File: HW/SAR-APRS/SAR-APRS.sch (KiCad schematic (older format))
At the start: 46 parts, among them J1 uFl, J2 Prog_header, J3 USB_B_Micro, Q1 2N7002, U1 DRA818V, U2 arduino_mini_clone, U3 NEO_GPS_MODULE, U4 HC-05, U5 TP4056

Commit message: update
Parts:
- removed D3, D4: LED, symbol device:LED
- removed R10: 100k, symbol device:R_Small
- added C12, C?: 100nF, symbol device:C_Small
- added C13: 10uF, symbol device:C_Small
- added D?: LED_BGRA, symbol device:LED_BGRA
- added D?: LED, symbol device:LED
- added J4: uFl, w_conn_rf:coaxial_u.fl-r-smt-1, symbol Connector:Conn_Coaxial
- added L4: L_Small, symbol device:L_Small
- added R19: 100, symbol device:R_Small
- added R?: 1k, symbol device:R_Small
- added U6: NEO-M8, symbol APRS_modules:NEO-M8
- added U?: EEPROM, symbol MLAB_IO:EEPROM
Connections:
- wire segments 166 -> 206
- no-connect marks 8 -> 17
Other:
- moved on the sheet: C1, C10, C11, C2, C3, C4, C5, C6, C7, C8, C9, D1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

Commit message: schematic update memmory adding
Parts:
- added C14: 100nF, symbol device:C_Small
- added U7: AT45DB641, Mlab_IO:SOIC-8_3.9x4.9mm_Pitch1.27mm, symbol APRS_modules:AT45DB081
- gave numbers to parts that had none: 5
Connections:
- wire segments 206 -> 222
- no-connect marks 17 -> 18
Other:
- moved on the sheet: C5
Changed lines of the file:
@@
 	6650 3525 6375 3525
 Wire Wire Line
-	5375 1600 6650 1600
-Wire Wire Line
-	5175 1600 4900 1600
+	5200 1600 6650 1600
+Wire Wire Line
+	5000 1600 4900 1600
 $Comp
 L device:C_Small C5
 U 1 1 5C01262D
-P 5275 1600
-F 0 "C5" H 5367 1646 50  0000 L CNN
-F 1 "10uF" H 5367 1555 50  0000 L CNN
-F 2 "" H 5275 1600 50  0001 C CNN
-F 3 "~" H 5275 1600 50  0001 C CNN
-	1    5275 1600
+P 5100 1600
+F 0 "C5" H 5192 1646 50  0000 L CNN
+F 1 "10uF" H 5192 1555 50  0000 L CNN
+F 2 "" H 5100 1600 50  0001 C CNN
+F 3 "~" H 5100 1600 50  0001 C CNN
+	1    5100 1600
 	0    -1   -1   0
 $EndComp
@@
 	6375 3125 6775 3125
 Wire Wire Line
-	6775 3125 6775 1600
-Wire Wire Line
-	6775 1600 9550 1600
-Wire Wire Line
-	9550 1600 9550 2525
+	6775 3125 6775 1775
+Wire Wire Line
+	6775 1775 9550 1775
+Wire Wire Line
+	9550 1775 9550 2525
 Wire Wire Line
 	8900 2525 9550 2525
@@
 Connection ~ 7500 5900
 $Comp
-L MLAB_IO:EEPROM U?
+L MLAB_IO:EEPROM U8
 U 1 1 5C17609F
 P 5825 6150
-F 0 "U?" H 5575 6550 60  0000 C CNN
+F 0 "U8" H 5575 6550 60  0000 C CNN
 F 1 "EEPROM" H 6150 6525 60  0000 C CNN
 F 2 "" H 5825 6150 60  0001 C CNN
@@
 $EndComp
 $Comp
-L device:LED_BGRA D?
+L device:LED_BGRA D4
 U 1 1 5C04ED53
 P 2275 6325
-F 0 "D?" V 2450 6650 50  0000 R CNN
+F 0 "D4" V 2450 6650 50  0000 R CNN
 F 1 "LED_BGRA" V 2275 7075 50  0000 R CNN
 F 2 "" H 2275 6275 50  0001 C CNN
@@
 	2725 6050 2825 6050
 $Comp
-L power:GND #PWR?
+L power:GND #PWR0134
 U 1 1 5C0E737B
 P 5825 6650
-F 0 "#PWR?" H 5825 6400 50  0001 C CNN
+F 0 "#PWR0134" H 5825 6400 50  0001 C CNN
 F 1 "GND" V 5830 6522 50  0000 R CNN
 F 2 "" H 5825 6650 50  0001 C CNN
@@
 $EndComp
 $Comp
-L power:+3V3 #PWR?
+L power:+3V3 #PWR0147
 U 1 1 5C0EEFDD
 P 5825 5500
-F 0 "#PWR?" H 5825 5350 50  0001 C CNN
+F 0 "#PWR0147" H 5825 5350 50  0001 C CNN
 F 1 "+3V3" H 5840 5673 50  0000 C CNN
 F 2 "" H 5825 5500 50  0001 C CNN
@@
 $EndComp
 $Comp
-L device:C_Small C?
+L device:C_Small C15
 U 1 1 5C0F65E9
 P 5600 5575
-F 0 "C?" H 5725 5650 50  0000 L CNN
+F 0 "C15" H 5725 5650 50  0000 L CNN
 F 1 "100nF" H 5675 5575 50  0000 L CNN
 F 2 "" H 5600 5575 50  0001 C CNN
@@
 	5825 5575 5825 5650
 $Comp
-L power:GND #PWR?
+L power:GND #PWR0148
 U 1 1 5C117D4C
 P 5500 5575
-F 0 "#PWR?" H 5500 5325 50  0001 C CNN
+F 0 "#PWR0148" H 5500 5325 50  0001 C CNN
 F 1 "GND" V 5505 5447 50  0000 R CNN
 F 2 "" H 5500 5575 50  0001 C CNN
@@
 	7950 5650 8025 5650
 $Comp
-L device:LED D?
+L device:LED D3
 U 1 1 5C189B26
 P 9750 5975
-F 0 "D?" V 9789 6053 50  0000 L CNN
+F 0 "D3" V 9789 6053 50  0000 L CNN
 F 1 "LED" V 9698 6053 50  0000 L CNN
 F 2 "" H 9750 5975 50  0001 C CNN
@@
 $EndComp
 $Comp
-L device:R_Small R?
+L device:R_Small R10
 U 1 1 5C193BD7
 P 9750 5725
-F 0 "R?" H 9600 5800 50  0000 L CNN
+F 0 "R10" H 9600 5800 50  0000 L CNN
 F 1 "1k" H 9600 5700 50  0000 L CNN
 F 2 "" H 9750 5725 50  0001 C CNN
@@
 $EndComp
 $Comp
-L power:GND #PWR?
+L power:GND #PWR0149
 U 1 1 5C199FCE
 P 9525 5150
-F 0 "#PWR?" H 9525 4900 50  0001 C CNN
+F 0 "#PWR0149" H 9525 4900 50  0001 C CNN
 F 1 "GND" V 9530 5022 50  0000 R CNN
 F 2 "" H 9525 5150 50  0001 C CNN
@@
 NoConn ~ 9525 5750
 $Comp
-L power:GND #PWR?
+L power:GND #PWR0150
 U 1 1 5C1E09BF
 P 9750 6125
-F 0 "#PWR?" H 9750 5875 50  0001 C CNN
+F 0 "#PWR0150" H 9750 5875 50  0001 C CNN
 F 1 "GND" V 9755 5997 50  0000 R CNN
 F 2 "" H 9750 6125 50  0001 C CNN
@@
 Wire Wire Line
 	8575 1900 8575 2425
+$Comp
+L power:GND #PWR0151
+U 1 1 5C1820F5
+P 8625 1175
+F 0 "#PWR0151" H 8625 925 50  0001 C CNN
+F 1 "GND" V 8625 1050 50  0000 R CNN
+F 2 "" H 8625 1175 50  0001 C CNN
+F 3 "" H 8625 1175 50  0001 C CNN
+	1    8625 1175
+	0    -1   1    0
+$EndComp
+$Comp
+L power:+3V3 #PWR0152
+U 1 1 5C18A0AD
+P 8875 1275
+F 0 "#PWR0152" H 8875 1125 50  0001 C CNN
+F 1 "+3V3" H 8890 1448 50  0000 C CNN
+F 2 "" H 8875 1275 50  0001 C CNN
+F 3 "" H 8875 1275 50  0001 C CNN
+	1    8875 1275
+	0    1    -1   0
+$EndComp
+$Comp
+L device:C_Small C14
+U 1 1 5C19098B
+P 8975 1550
+F 0 "C14" H 9067 1596 50  0000 L CNN
+F 1 "100nF" V 9125 1250 50  0000 L CNN
+F 2 "" H 8975 1550 50  0001 C CNN
+F 3 "~" H 8975 1550 50  0001 C CNN
+	1    8975 1550
+	0    -1   1    0
+$EndComp
+$Comp
+L power:GND #PWR0153
+U 1 1 5C245DAA
+P 7525 1375
+F 0 "#PWR0153" H 7525 1125 50  0001 C CNN
+F 1 "GND" V 7525 1225 50  0000 R CNN
+F 2 "" H 7525 1375 50  0001 C CNN
+F 3 "" H 7525 1375 50  0001 C CNN
+	1    7525 1375
+	0    1    -1   0
+$EndComp
+Wire Wire Line
+	6375 2925 6500 2925
+Wire Wire Line
+	5475 3025 5350 3025
+$Comp
+L APRS_modules:AT45DB081 U7
+U 1 1 5C2A166A
+P 8075 1225
+F 0 "U7" H 8075 1640 50  0000 C CNN
+F 1 "AT45DB641" H 8075 1549 50  0000 C CNN
+F 2 "Mlab_IO:SOIC-8_3.9x4.9mm_Pitch1.27mm" H 7525 1475 50  0001 C CNN
+F 3 "" H 7525 1475 50  0001 C CNN
+	1    8075 1225
+	1    0    0    -1
+$EndComp
+NoConn ~ 8625 1375
+Wire Wire Line
+	8625 1275 8800 1275
+Wire Wire Line
+	8875 1550 8800 1550
+Connection ~ 8800 1275
+Wire Wire Line
+	8800 1275 8875 1275
+$Comp
+L power:GND #PWR0154
+U 1 1 5C302407
+P 9075 1550
+F 0 "#PWR0154" H 9075 1300 50  0001 C CNN
+F 1 "GND" V 9075 1425 50  0000 R CNN
+F 2 "" H 9075 1550 50  0001 C CNN
+F 3 "" H 9075 1550 50  0001 C CNN
+	1    9075 1550
+	0    -1   1    0
+$EndComp
+Wire Wire Line
+	7525 1275 7175 1275
+Wire Wire Line
+	7175 1275 7175 1550
+Wire Wire Line
+	7175 1550 8800 1550
+Connection ~ 8800 1550
+Wire Wire Line
+	8800 1550 8800 1275
+Wire Wire Line
+	6500 1175 7525 1175
+Wire Wire Line
+	7525 1075 5475 1075
+Wire Wire Line
+	5350 750  8625 750
+Wire Wire Line
+	8625 750  8625 1075
+Wire Wire Line
+	5350 750  5350 3025
+Wire Wire Line
+	5475 1075 5475 2925
+Wire Wire Line
+	6500 1175 6500 2925
 $EndSCHEMATC

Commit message: schematic update
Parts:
- removed R15: ?, symbol device:R_Small
- removed R16: 1k, symbol device:R_Small
- removed U5: TP4056, symbol APRS_modules:TP4056
- added C? (x2): 100nF, symbol device:C_Small
- added Q? (x2): 2N7002, TO_SOT_Packages_SMD:SOT-23, symbol Transistor:2N7002
- added R?: 100, symbol device:R_Small
- added R?: 1k, symbol device:R_Small
- added U?: DW01x, symbol APRS_modules:DW01x
- added U?: TP4056, symbol APRS_modules:TP4056
- R14: value 1k -> 1k2
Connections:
- net labels removed: Temp
- wire segments 222 -> 231
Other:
- moved on the sheet: C10, C11, D4, J3, R13, R14, R17, R18

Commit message: schematic update
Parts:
- removed C10: 10uF, symbol device:C_Small
- added C10, C18: 10uF, symbol device:CP1_Small
- added D5: 1N5818, Diode_THT:D_DO-41_SOD81_P10.16mm_Horizontal, symbol Diode:1N5818
- added L5: 22uH, symbol device:L_Small
- added R20: ?, symbol device:R_Small
- added R21: 2k4, symbol device:R_Small
- added R22: 1k5, symbol device:R_Small
- added U10: ADP1108AN-3.3, Housings_DIP:DIP-8_W7.62mm, symbol dc-dc:ADP1108AN-3.3
- gave numbers to parts that had none: 8
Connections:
- net labels removed: +3V8
- wire segments 231 -> 255
- no-connect marks 18 -> 21
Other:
- moved on the sheet: C1, C11, C12, C13, C14, C15, C16, C17, C2, C3, C4, C5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

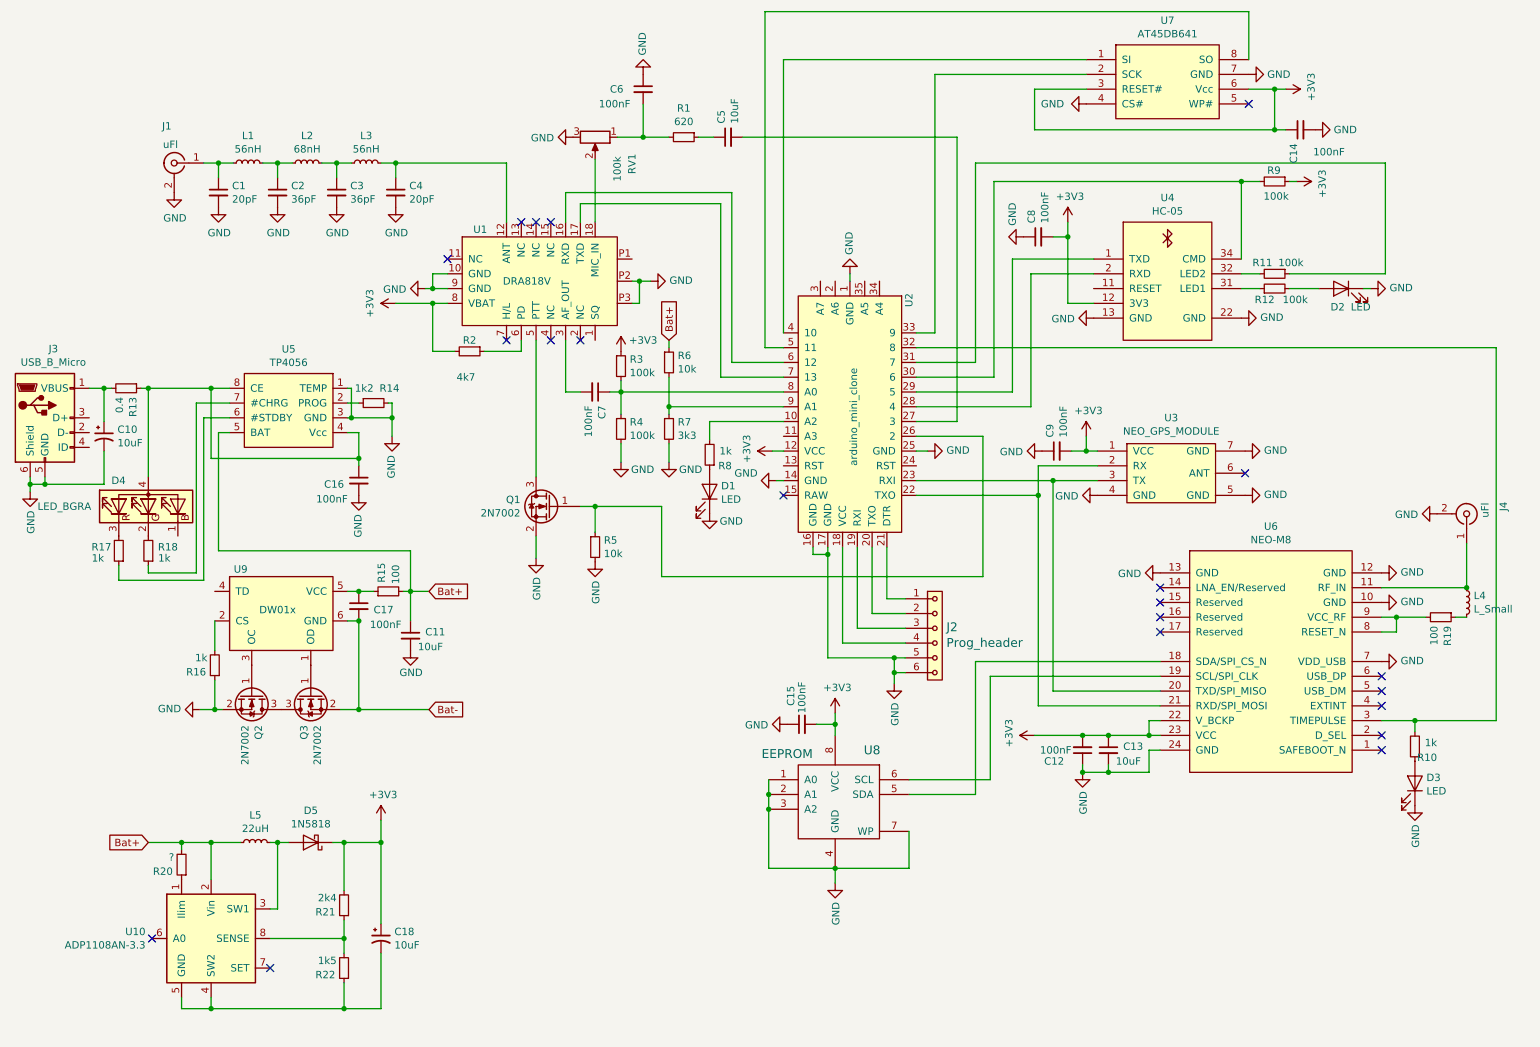
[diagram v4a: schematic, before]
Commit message: schematic update
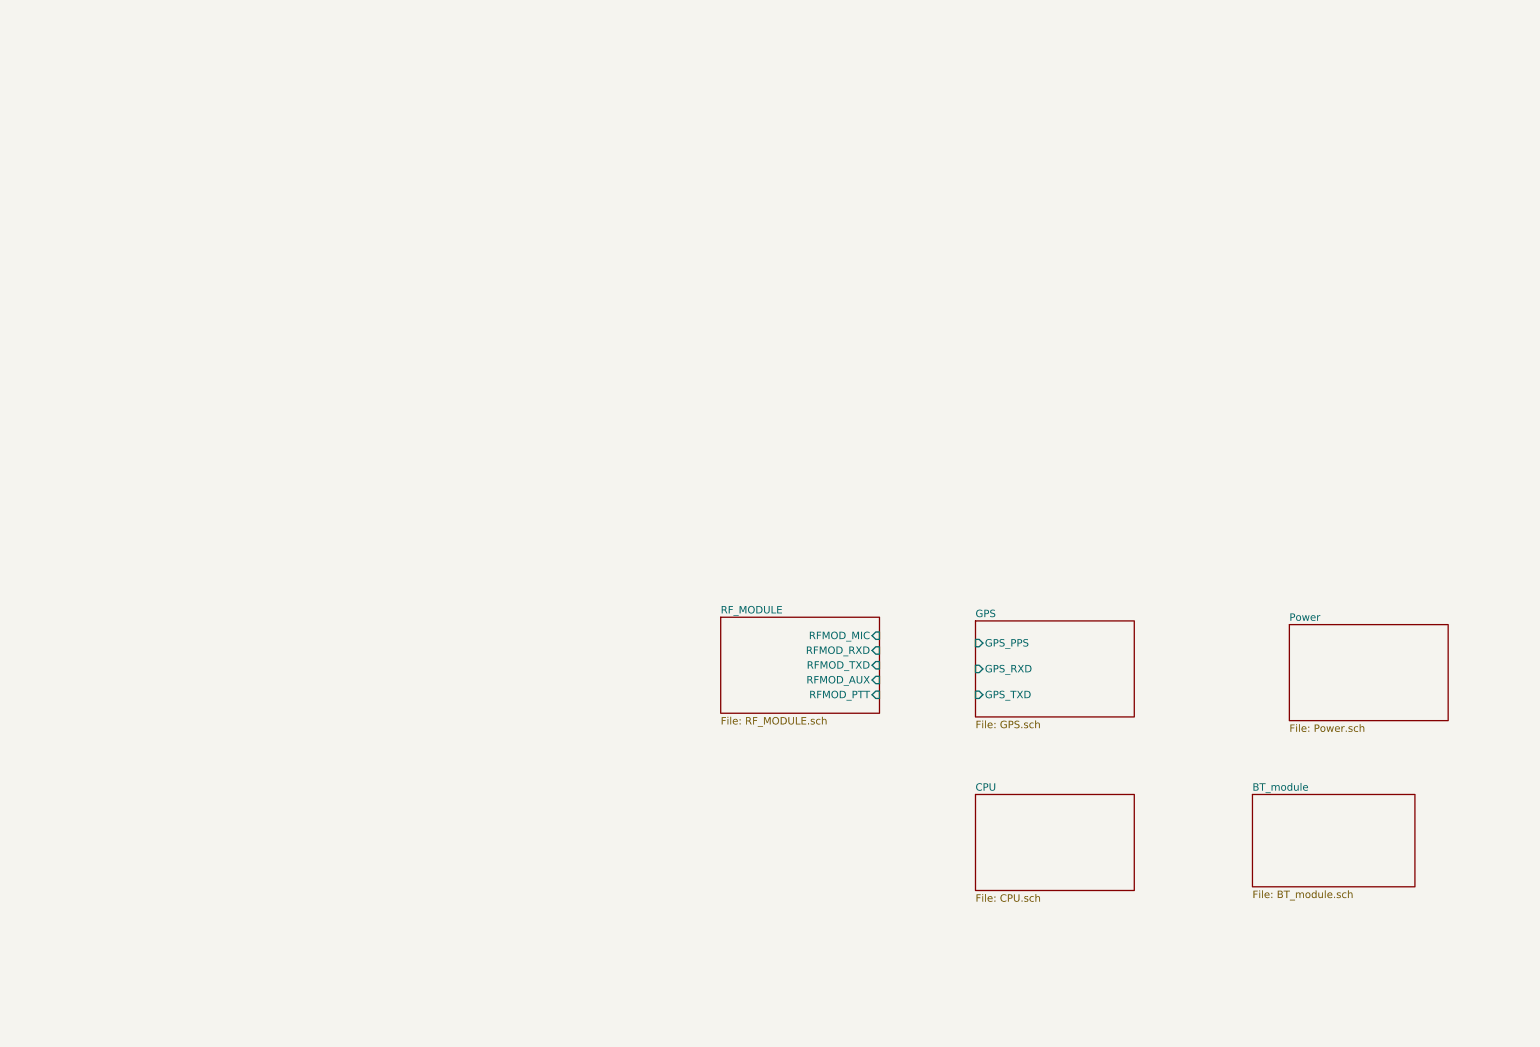
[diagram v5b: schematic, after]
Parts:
- removed C1, C4: 20pF, symbol device:C_Small
- removed C10, C18: 10uF, symbol device:CP1_Small
- removed C11, C13, C5: 10uF, symbol device:C_Small
- removed C12, C14, C15, C16, C17, C6, C7, C8, C9: 100nF, symbol device:C_Small
- removed C2, C3: 36pF, symbol device:C_Small
- removed D1, D2, D3: LED, symbol device:LED
- removed D4: LED_BGRA, symbol device:LED_BGRA
- removed D5: 1N5818, Diode_THT:D_DO-41_SOD81_P10.16mm_Horizontal, symbol Diode:1N5818
- removed J1, J4: uFl, w_conn_rf:coaxial_u.fl-r-smt-1, symbol Connector:Conn_Coaxial
- removed J2: Prog_header, symbol MLAB_HEADER:HEADER_1x06
- removed J3: USB_B_Micro, symbol Connector:USB_B_Micro
- removed L1, L3: 56nH, symbol device:L_Small
- removed L2: 68nH, symbol device:L_Small
- removed L4: L_Small, symbol device:L_Small
- removed L5: 22uH, symbol device:L_Small
- removed Q1, Q2, Q3: 2N7002, TO_SOT_Packages_SMD:SOT-23, symbol Transistor:2N7002
- removed R1: 620, symbol device:R_Small
- removed R10, R16, R17, R18, R8: 1k, symbol device:R_Small
- removed R11, R12, R3, R4, R9: 100k, symbol device:R_Small
- removed R13: 0.4, symbol device:R_Small
- removed R14: 1k2, symbol device:R_Small
- removed R15, R19: 100, symbol device:R_Small
- removed R2: 4k7, symbol device:R_Small
- removed R20: ?, symbol device:R_Small
- removed R21: 2k4, symbol device:R_Small
- removed R22: 1k5, symbol device:R_Small
- removed R5, R6: 10k, symbol device:R_Small
- removed R7: 3k3, symbol device:R_Small
- removed RV1: 100k, symbol device:R_POT
- removed U1: DRA818V, APRS_modules:DRA818, symbol APRS_modules:DRA818V
- removed U10: ADP1108AN-3.3, Housings_DIP:DIP-8_W7.62mm, symbol dc-dc:ADP1108AN-3.3
- removed U2: arduino_mini_clone, APRS_modules:arduino_mini_clone, symbol APRS_modules:arduino_mini_clone
- removed U3: NEO_GPS_MODULE, symbol APRS_modules:NEO_GPS_MODULE
- removed U4: HC-05, maxrez:HC-05 BT, symbol APRS_modules:HC-05
- removed U5: TP4056, symbol APRS_modules:TP4056
- removed U6: NEO-M8, symbol APRS_modules:NEO-M8
- removed U7: AT45DB641, Mlab_IO:SOIC-8_3.9x4.9mm_Pitch1.27mm, symbol APRS_modules:AT45DB081
- removed U8: EEPROM, symbol MLAB_IO:EEPROM
- removed U9: DW01x, symbol APRS_modules:DW01x
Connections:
- no-connect marks 21 -> 0
